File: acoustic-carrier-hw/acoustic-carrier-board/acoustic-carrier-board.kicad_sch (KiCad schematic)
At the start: 0 parts

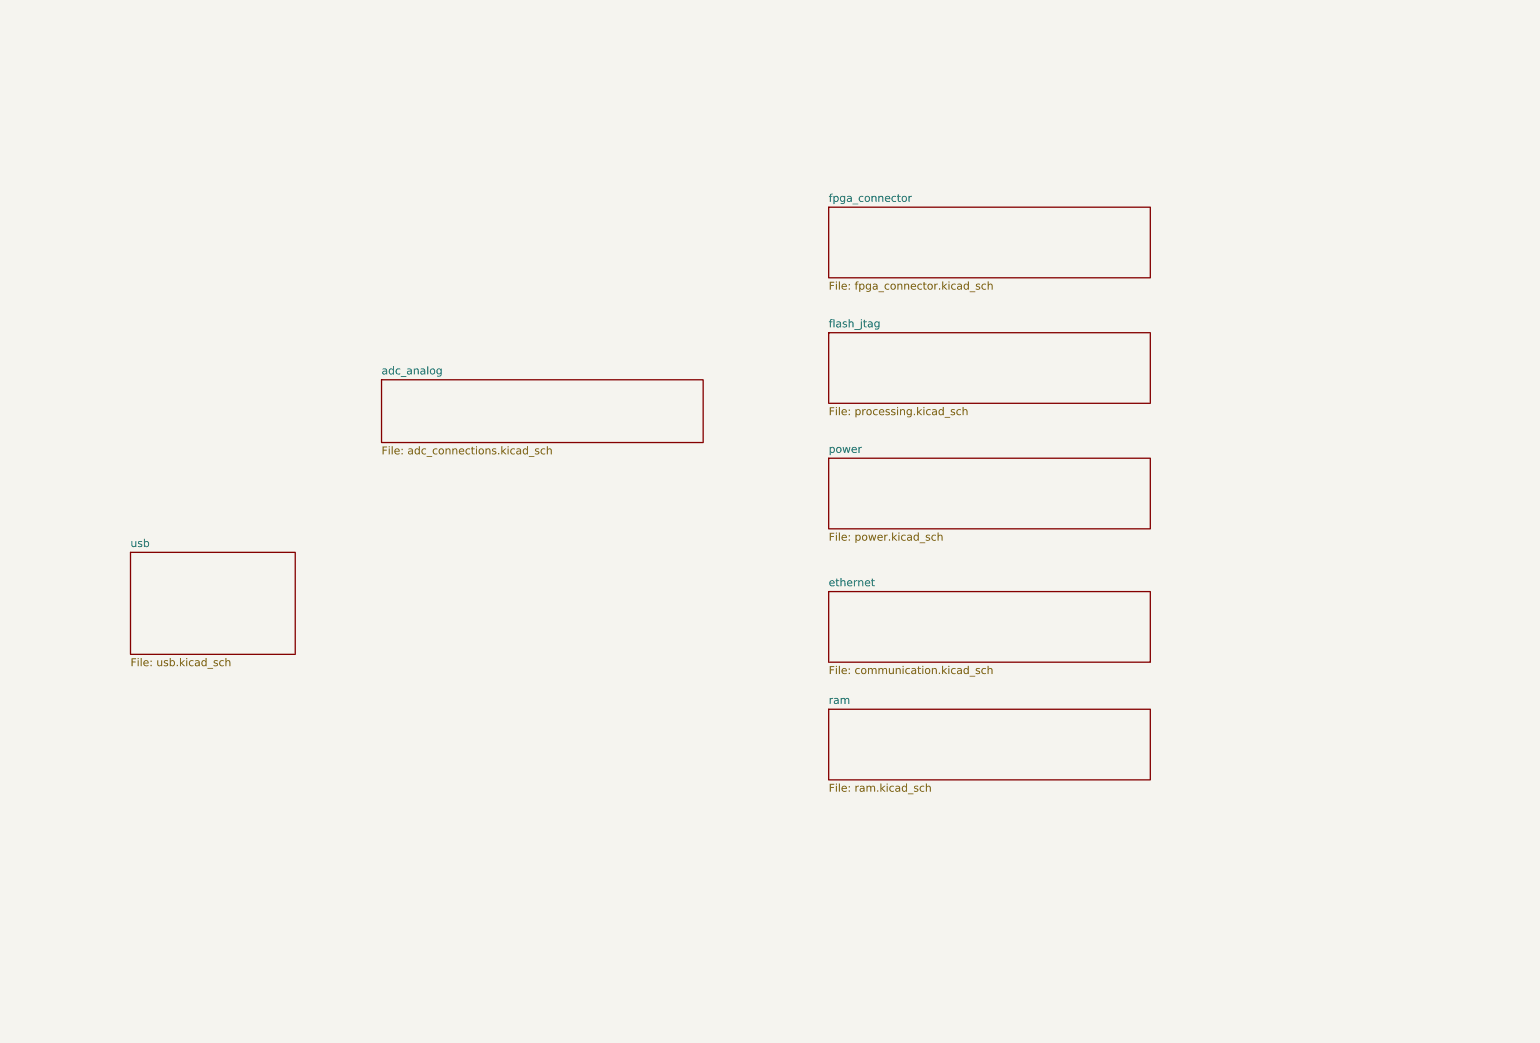
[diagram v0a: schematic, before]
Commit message: [¢arrier] Fixed busses, added resistive arrays instead of 4x4k7 or 4x10k
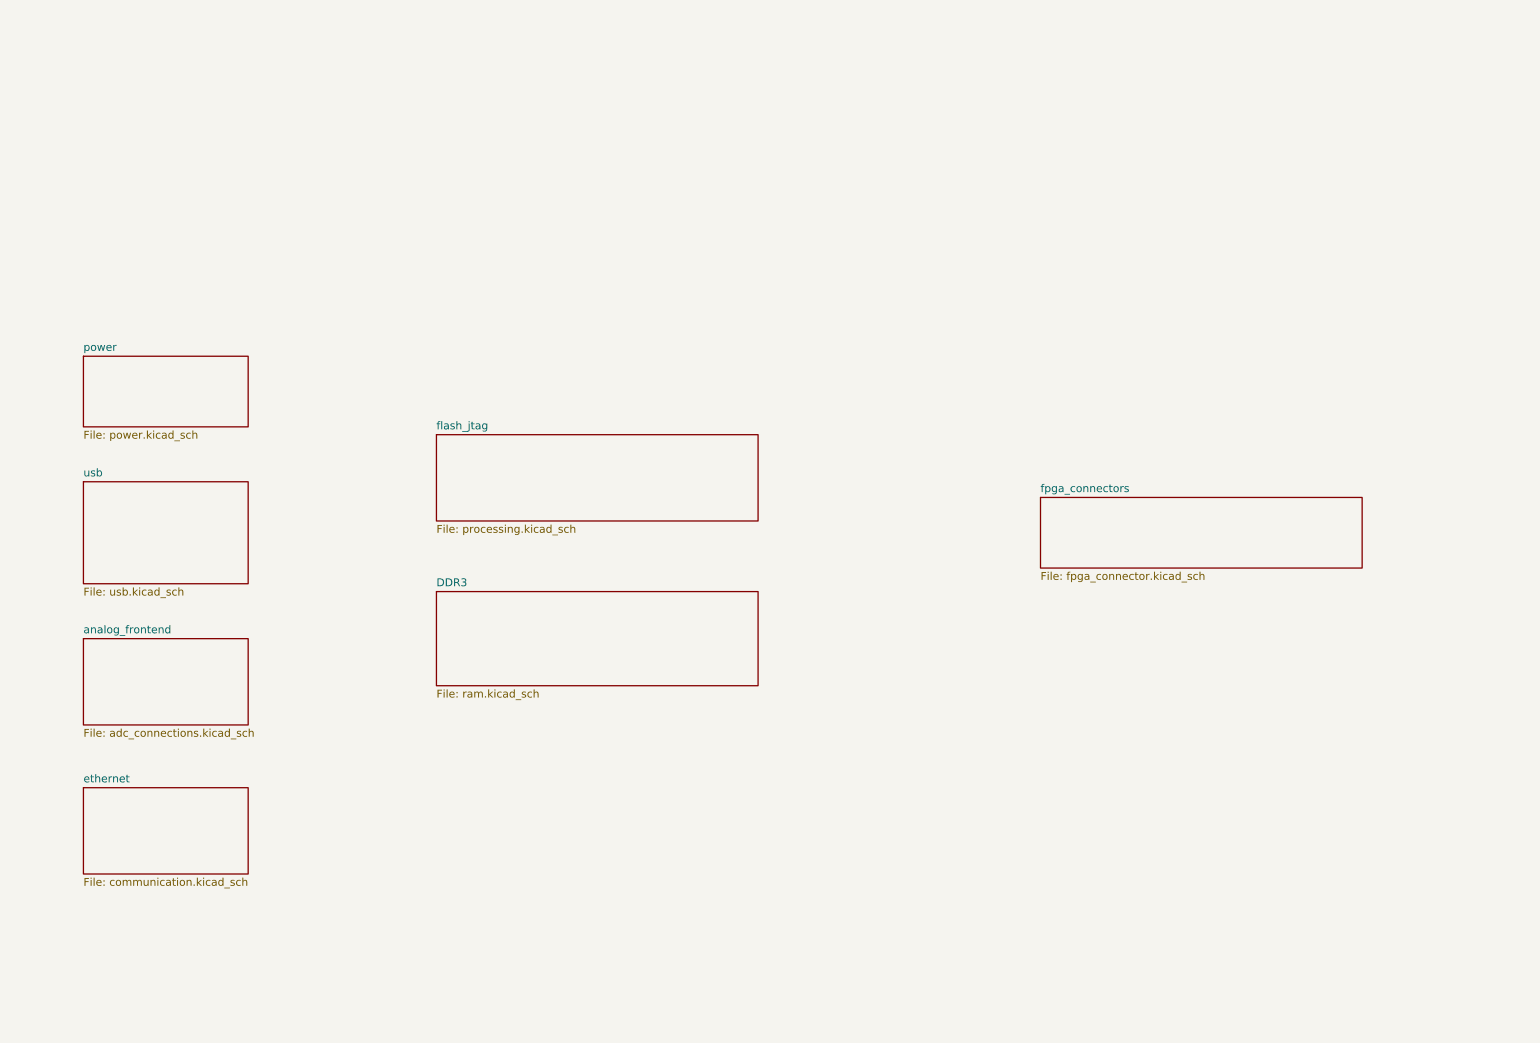
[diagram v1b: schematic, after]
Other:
- sheet adc_analog renamed analog_frontend
- sheet fpga_connector renamed fpga_connectors
- sheet ram renamed DDR3

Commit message: [carrier] Added separate schematics for banks
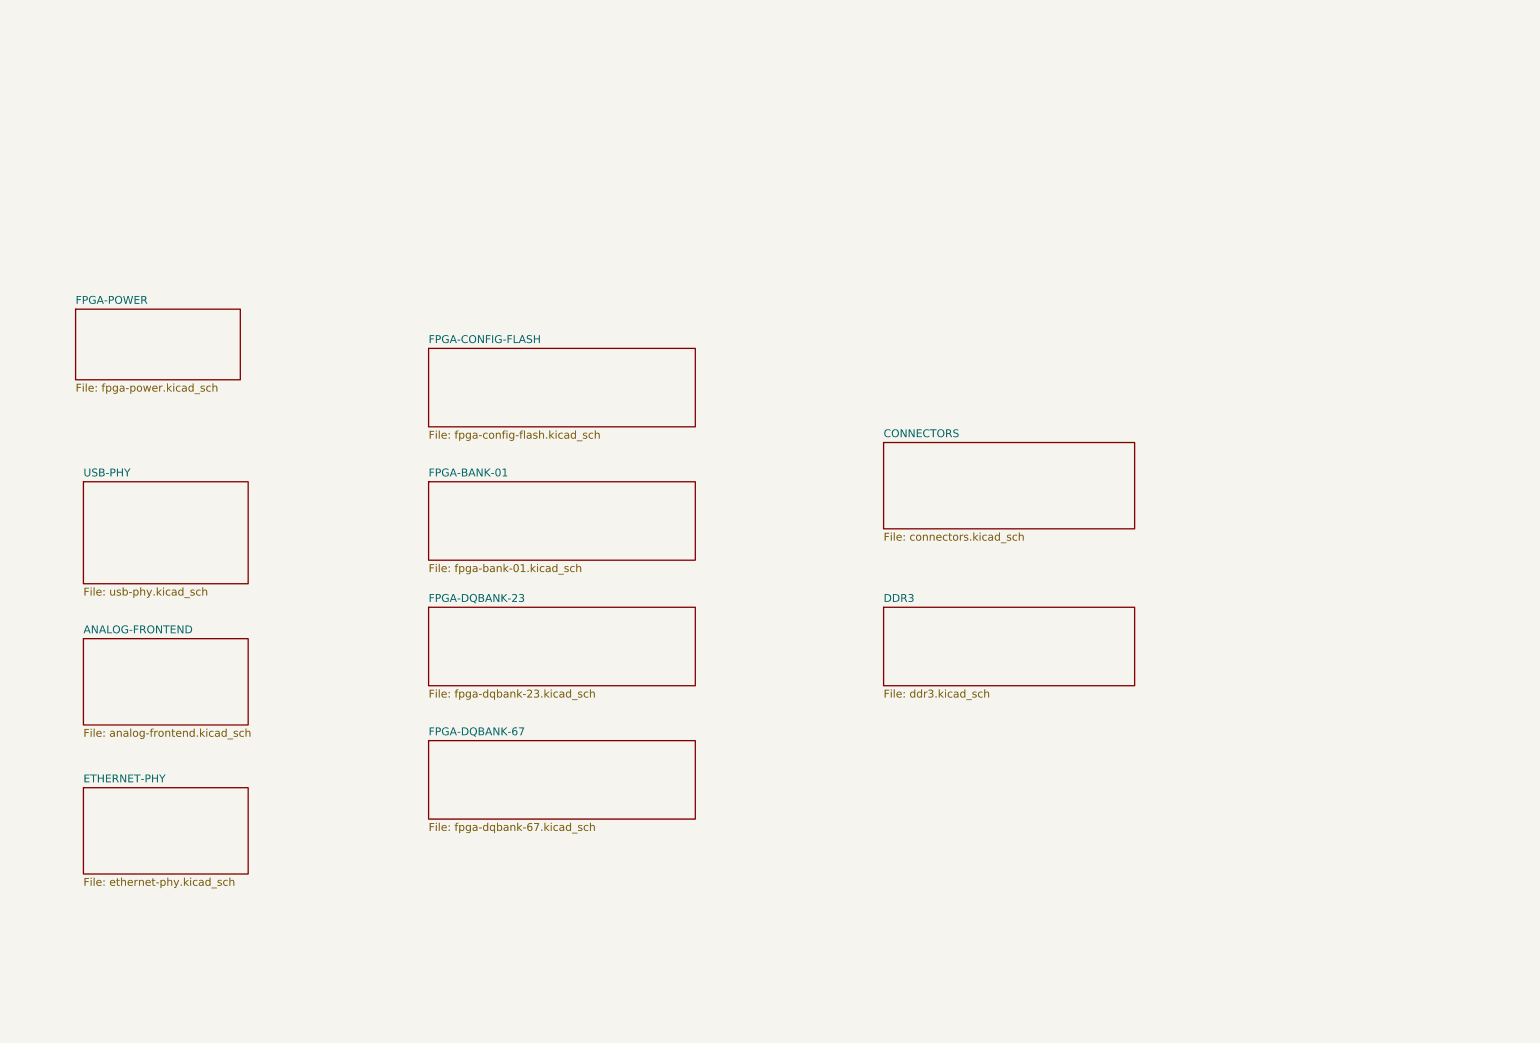
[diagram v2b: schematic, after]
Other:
- sheet analog_frontend renamed ANALOG-FRONTEND
- sheet ethernet renamed ETHERNET-PHY
- sheet flash_jtag renamed FPGA-CONFIG-FLASH
- sheet fpga_connectors renamed CONNECTORS
- sheet power renamed FPGA-POWER
- sheet usb renamed USB-PHY
- added sheet FPGA-BANK-01 (fpga-bank-01.kicad_sch)
- added sheet FPGA-DQBANK-23 (fpga-dqbank-23.kicad_sch)
- added sheet FPGA-DQBANK-67 (fpga-dqbank-67.kicad_sch)
- sheet ANALOG-FRONTEND: file adc_connections.kicad_sch -> analog-frontend.kicad_sch
- sheet CONNECTORS: file fpga_connector.kicad_sch -> connectors.kicad_sch
- sheet DDR3: file ram.kicad_sch -> ddr3.kicad_sch
- sheet ETHERNET-PHY: file communication.kicad_sch -> ethernet-phy.kicad_sch
- sheet FPGA-CONFIG-FLASH: file processing.kicad_sch -> fpga-config-flash.kicad_sch
- sheet FPGA-POWER: file power.kicad_sch -> fpga-power.kicad_sch
- sheet USB-PHY: file usb.kicad_sch -> usb-phy.kicad_sch
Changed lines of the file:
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@@
 	(paper "A4")
 	(sheet
-		(at 91.44 53.34)
-		(size 52.07 13.97)
-		(exclude_from_sim no)
-		(in_bom yes)
-		(on_board yes)
-		(dnp no)
-		(fields_autoplaced yes)
-		(stroke
-			(width 0.1524)
-			(type solid)
-		)
-		(fill
-			(color 0 0 0 0.0000)
-		)
-		(property "Sheetname" "flash_jtag"
-			(at 91.44 52.6284 0)
-			(effects
-				(font
-					(size 1.27 1.27)
-				)
-				(justify left bottom)
-			)
-		)
-		(property "Sheetfile" "processing.kicad_sch"
-			(at 91.44 67.8946 0)
+		(at 90.17 39.37)
+		(size 43.18 12.7)
+		(exclude_from_sim no)
+		(in_bom yes)
+		(on_board yes)
+		(dnp no)
+		(fields_autoplaced yes)
+		(stroke
+			(width 0.1524)
+			(type solid)
+		)
+		(fill
+			(color 0 0 0 0.0000)
+		)
+		(property "Sheetname" "FPGA-CONFIG-FLASH"
+			(at 90.17 38.6584 0)
+			(effects
+				(font
+					(size 1.27 1.27)
+				)
+				(justify left bottom)
+			)
+		)
+		(property "Sheetfile" "fpga-config-flash.kicad_sch"
+			(at 90.17 52.6546 0)
 			(effects
 				(font
@@
 				(path "/25b015c9-ab13-4427-b72c-b6f348597100"
 					(page "4")
+				)
+			)
+		)
+	)
+	(sheet
+		(at 90.17 60.96)
+		(size 43.18 12.7)
+		(exclude_from_sim no)
+		(in_bom yes)
+		(on_board yes)
+		(dnp no)
+		(fields_autoplaced yes)
+		(stroke
+			(width 0.1524)
+			(type solid)
+		)
+		(fill
+			(color 0 0 0 0.0000)
+		)
+		(property "Sheetname" "FPGA-BANK-01"
+			(at 90.17 60.2484 0)
+			(effects
+				(font
+					(size 1.27 1.27)
+				)
+				(justify left bottom)
+			)
+		)
+		(property "Sheetfile" "fpga-bank-01.kicad_sch"
+			(at 90.17 74.2446 0)
+			(effects
+				(font
+					(size 1.27 1.27)
+				)
+				(justify left top)
+			)
+		)
+		(instances
+			(project "acoustic-carrier-board"
+				(path "/25b015c9-ab13-4427-b72c-b6f348597100"
+					(page "9")
 				)
 			)
@@
 			(color 0 0 0 0.0000)
 		)
-		(property "Sheetname" "analog_frontend"
+		(property "Sheetname" "ANALOG-FRONTEND"
 			(at 34.29 85.6484 0)
 			(effects
@@
 			)
 		)
-		(property "Sheetfile" "adc_connections.kicad_sch"
+		(property "Sheetfile" "analog-frontend.kicad_sch"
 			(at 34.29 100.9146 0)
 			(effects
@@
 	)
 	(sheet
-		(at 34.29 40.64)
+		(at 90.17 102.87)
+		(size 43.18 12.7)
+		(exclude_from_sim no)
+		(in_bom yes)
+		(on_board yes)
+		(dnp no)
+		(fields_autoplaced yes)
+		(stroke
+			(width 0.1524)
+			(type solid)
+		)
+		(fill
+			(color 0 0 0 0.0000)
+		)
+		(property "Sheetname" "FPGA-DQBANK-67"
+			(at 90.17 102.1584 0)
+			(effects
+				(font
+					(size 1.27 1.27)
+				)
+				(justify left bottom)
+			)
+		)
+		(property "Sheetfile" "fpga-dqbank-67.kicad_sch"
+			(at 90.17 116.1546 0)
+			(effects
+				(font
+					(size 1.27 1.27)
+				)
+				(justify left top)
+			)
+		)
+		(instances
+			(project "acoustic-carrier-board"
+				(path "/25b015c9-ab13-4427-b72c-b6f348597100"
+					(page "11")
+				)
+			)
+		)
+	)
+	(sheet
+		(at 33.02 33.02)
 		(size 26.67 11.43)
 		(exclude_from_sim no)
@@
 			(color 0 0 0 0.0000)
 		)
-		(property "Sheetname" "power"
-			(at 34.29 39.9284 0)
-			(effects
-				(font
-					(size 1.27 1.27)
-				)
-				(justify left bottom)
-			)
-		)
-		(property "Sheetfile" "power.kicad_sch"
-			(at 34.29 52.6546 0)
+		(property "Sheetname" "FPGA-POWER"
+			(at 33.02 32.3084 0)
+			(effects
+				(font
+					(size 1.27 1.27)
+				)
+				(justify left bottom)
+			)
+		)
+		(property "Sheetfile" "fpga-power.kicad_sch"
+			(at 33.02 45.0346 0)
 			(effects
 				(font
@@
 		)
 		(property "Field2" ""
-			(at 34.29 40.64 0)
+			(at 33.02 33.02 0)
 			(effects
 				(font
@@
 	)
 	(sheet
-		(at 189.23 63.5)
-		(size 52.07 11.43)
-		(exclude_from_sim no)
-		(in_bom yes)
-		(on_board yes)
-		(dnp no)
-		(fields_autoplaced yes)
-		(stroke
-			(width 0.1524)
-			(type solid)
-		)
-		(fill
-			(color 0 0 0 0.0000)
-		)
-		(property "Sheetname" "fpga_connectors"
-			(at 189.23 62.7884 0)
-			(effects
-				(font
-					(size 1.27 1.27)
-				)
-				(justify left bottom)
-			)
-		)
-		(property "Sheetfile" "fpga_connector.kicad_sch"
-			(at 189.23 75.5146 0)
+		(at 90.17 81.28)
+		(size 43.18 12.7)
+		(exclude_from_sim no)
+		(in_bom yes)
+		(on_board yes)
+		(dnp no)
+		(fields_autoplaced yes)
+		(stroke
+			(width 0.1524)
+			(type solid)
+		)
+		(fill
+			(color 0 0 0 0.0000)
+		)
+		(property "Sheetname" "FPGA-DQBANK-23"
+			(at 90.17 80.5684 0)
+			(effects
+				(font
+					(size 1.27 1.27)
+				)
+				(justify left bottom)
+			)
+		)
+		(property "Sheetfile" "fpga-dqbank-23.kicad_sch"
+			(at 90.17 94.5646 0)
+			(effects
+				(font
+					(size 1.27 1.27)
+				)
+				(justify left top)
+			)
+		)
+		(instances
+			(project "acoustic-carrier-board"
+				(path "/25b015c9-ab13-4427-b72c-b6f348597100"
+					(page "10")
+				)
+			)
+		)
+	)
+	(sheet
+		(at 163.83 54.61)
+		(size 40.64 13.97)
+		(exclude_from_sim no)
+		(in_bom yes)
+		(on_board yes)
+		(dnp no)
+		(fields_autoplaced yes)
+		(stroke
+			(width 0.1524)
+			(type solid)
+		)
+		(fill
+			(color 0 0 0 0.0000)
+		)
+		(property "Sheetname" "CONNECTORS"
+			(at 163.83 53.8984 0)
+			(effects
+				(font
+					(size 1.27 1.27)
+				)
+				(justify left bottom)
+			)
+		)
+		(property "Sheetfile" "connectors.kicad_sch"
+			(at 163.83 69.1646 0)
 			(effects
 				(font
@@
 			(color 0 0 0 0.0000)
 		)
-		(property "Sheetname" "usb"
+		(property "Sheetname" "USB-PHY"
 			(at 34.29 60.2484 0)
 			(effects
@@
 			)
 		)
-		(property "Sheetfile" "usb.kicad_sch"
+		(property "Sheetfile" "usb-phy.kicad_sch"
 			(at 34.29 78.0546 0)
 			(effects
@@
 			(color 0 0 0 0.0000)
 		)
-		(property "Sheetname" "ethernet"
+		(property "Sheetname" "ETHERNET-PHY"
 			(at 34.29 109.7784 0)
 			(effects
@@
 			)
 		)
-		(property "Sheetfile" "communication.kicad_sch"
+		(property "Sheetfile" "ethernet-phy.kicad_sch"
 			(at 34.29 125.0446 0)
 			(effects
@@
 	)
 	(sheet
-		(at 91.44 78.74)
-		(size 52.07 15.24)
+		(at 163.83 81.28)
+		(size 40.64 12.7)
 		(exclude_from_sim no)
 		(in_bom yes)
@@
 		)
 		(property "Sheetname" "DDR3"
-			(at 91.44 78.0284 0)
-			(effects
-				(font
-					(size 1.27 1.27)
-				)
-				(justify left bottom)
-			)
-		)
-		(property "Sheetfile" "ram.kicad_sch"
-			(at 91.44 94.5646 0)
+			(at 163.83 80.5684 0)
+			(effects
+				(font
+					(size 1.27 1.27)
+				)
+				(justify left bottom)
+			)
+		)
+		(property "Sheetfile" "ddr3.kicad_sch"
+			(at 163.83 94.5646 0)
 			(effects
 				(font
@@
 		)
 		(property "Field2" ""
-			(at 91.44 78.74 0)
-			(effects
-				(font
+			(at 163.83 81.28 0)
+			(effects
+				(font

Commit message: [carrier] Added hierarchical labels
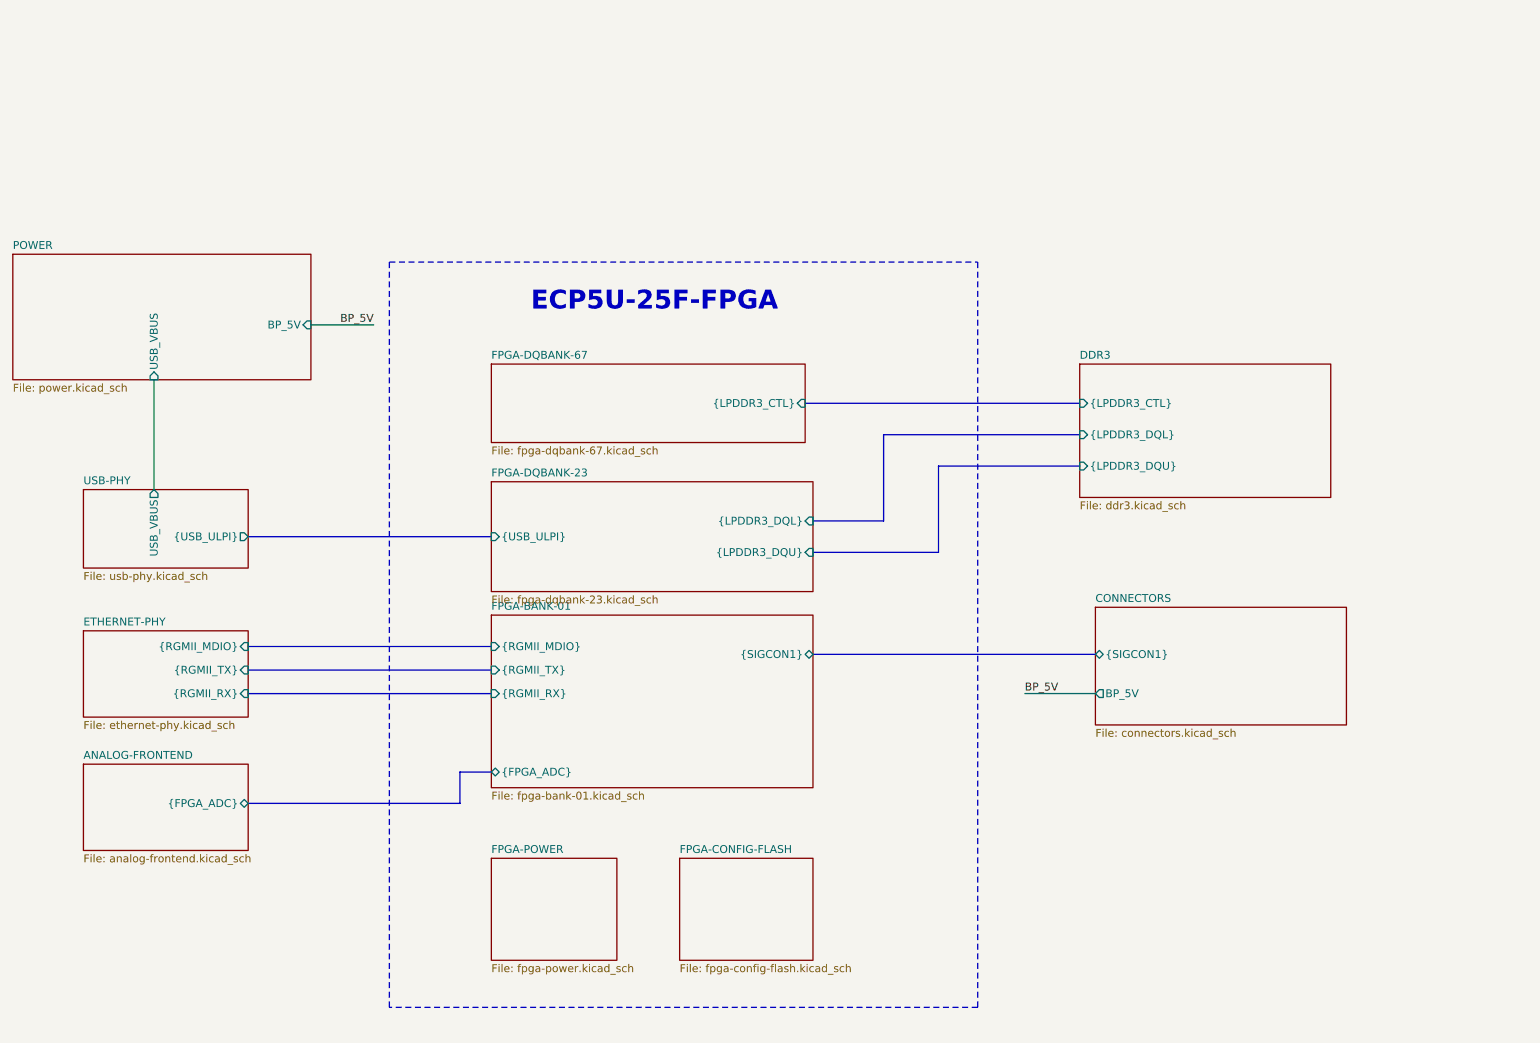
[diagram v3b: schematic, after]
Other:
- added sheet POWER (power.kicad_sch)
- sheet ANALOG-FRONTEND ports: added {FPGA_ADC}; removed none
- sheet CONNECTORS ports: added BP_5V, {SIGCON1}; removed none
- sheet DDR3 ports: added {LPDDR3_CTL}, {LPDDR3_DQL}, {LPDDR3_DQU}; removed none
- sheet ETHERNET-PHY ports: added {RGMII_MDIO}, {RGMII_RX}, {RGMII_TX}; removed none
- sheet FPGA-BANK-01 ports: added {FPGA_ADC}, {RGMII_MDIO}, {RGMII_RX}, {RGMII_TX}, {SIGCON1}; removed none
- sheet FPGA-DQBANK-23 ports: added {LPDDR3_DQL}, {LPDDR3_DQU}, {USB_ULPI}; removed none
- sheet FPGA-DQBANK-67 ports: added {LPDDR3_CTL}; removed none
- sheet USB-PHY ports: added USB_VBUS, {USB_ULPI}; removed none
- note added: "ECP5U-25F-FPGA"
